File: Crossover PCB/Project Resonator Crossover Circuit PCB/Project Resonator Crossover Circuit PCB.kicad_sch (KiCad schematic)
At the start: 24 parts

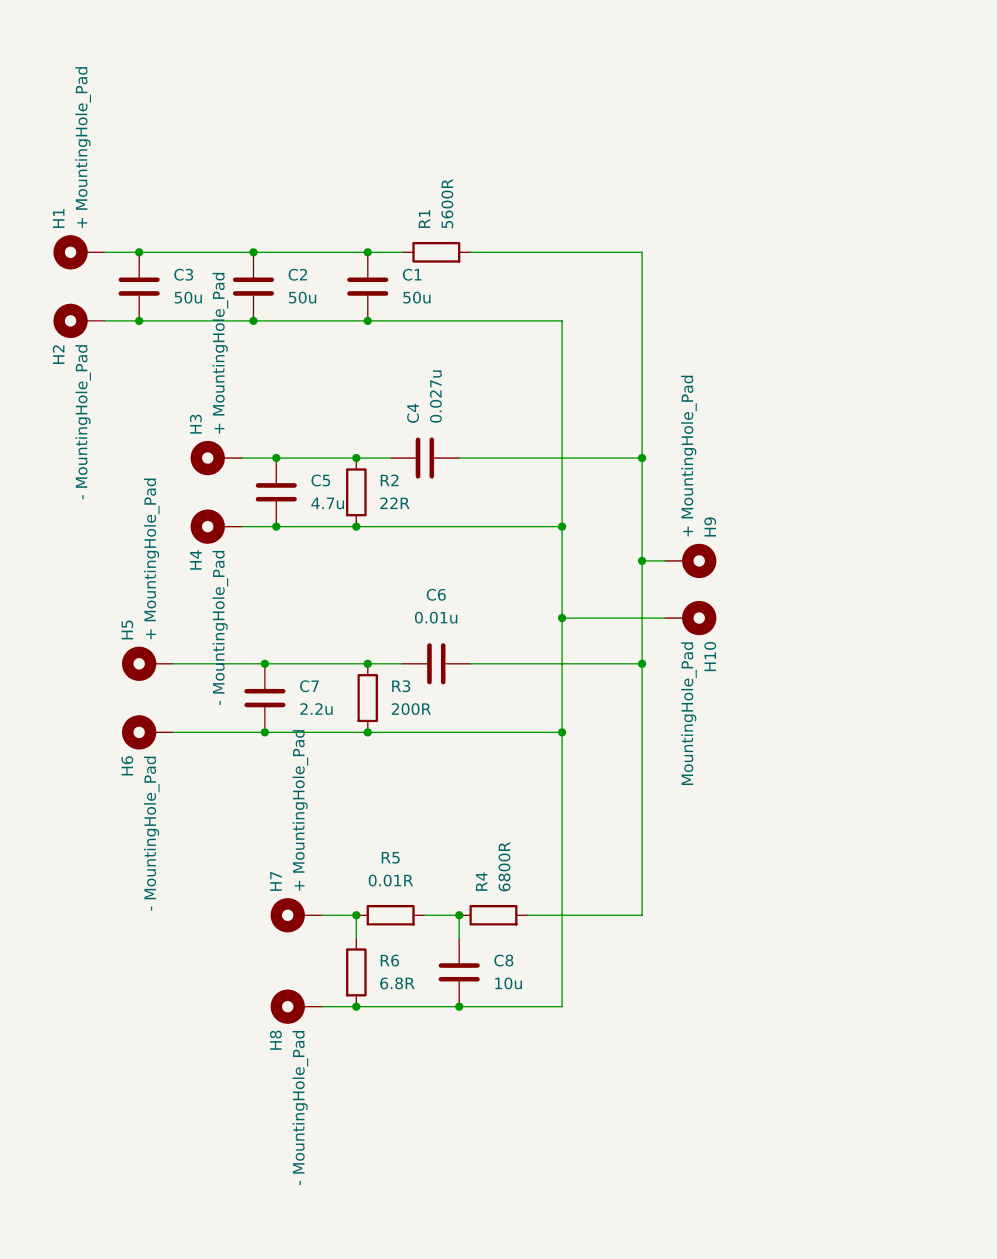
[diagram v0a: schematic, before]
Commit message: MAJOR UPDATE: Improved Crossover to reduce redudent componets from 15 -> 10, Improved subbass isolation, updated PCB to reflect changes, added v3 shell images to assets, uploaded new gerber and drill files
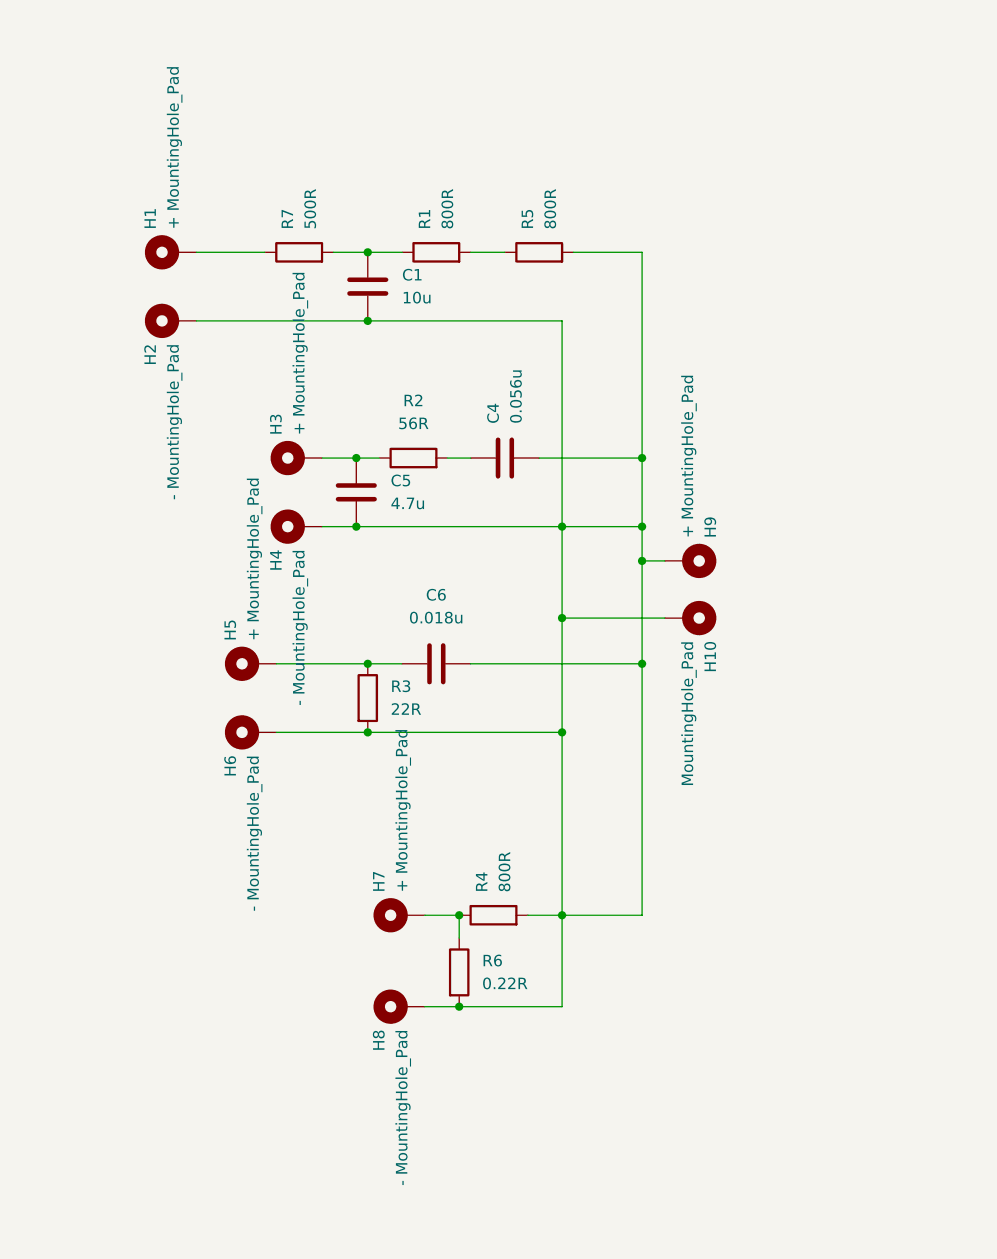
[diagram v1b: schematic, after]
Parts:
- removed C2, C3: 50u, Capacitor_SMD:C_0402_1005Metric_Pad0.74x0.62mm_HandSolder, symbol Device:C
- removed C7: 2.2u, Capacitor_SMD:C_0402_1005Metric_Pad0.74x0.62mm_HandSolder, symbol Device:C
- removed C8: 10u, Capacitor_SMD:C_0402_1005Metric_Pad0.74x0.62mm_HandSolder, symbol Device:C
- added R7: 500R, Resistor_SMD:R_0402_1005Metric_Pad0.72x0.64mm_HandSolder, symbol Device:R
- C1: value 50u -> 10u
- C4: value 0.027u -> 0.056u
- C6: value 0.01u -> 0.018u
- R1: value 5600R -> 800R
- R2: value 22R -> 56R
- R3: value 200R -> 22R
- R4: value 6800R -> 800R
- R5: value 0.01R -> 800R
- R6: value 6.8R -> 0.22R
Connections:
- net at C1.2, C5.2, H10.1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: now also C4.2, C6.2, H9.1, R4.2, R5.2; no longer R2.2
- net at H7.1, R6.1: now also R4.1; no longer R5.1
- net at C5.1, H3.1, R2.1: no longer C4.1
- net at C1.1, R1.1: now also R7.2; no longer H1.1
- new net: C4.1, R2.2
- new net: H1.1, R7.1
- new net: R1.2, R5.1
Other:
- moved on the sheet: C4, C5, H1, H2, H3, H4, H5, H6, H7, H8, R2, R6

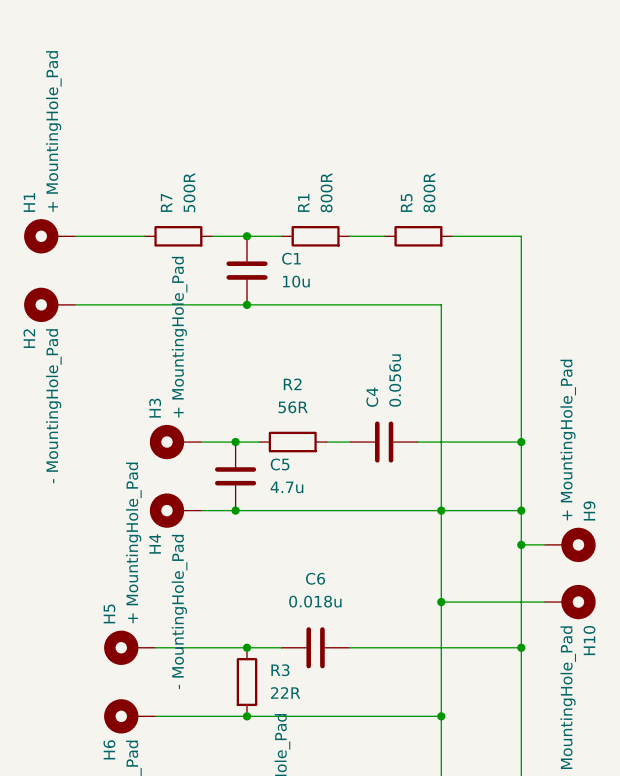
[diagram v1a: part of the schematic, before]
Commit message: updated crossover to have ~5-6db cut at 10k to match shell material high frequency resonace (updated CROSSOVER, SCHEMATIC, PCB, GERBER, and DRILL FILES
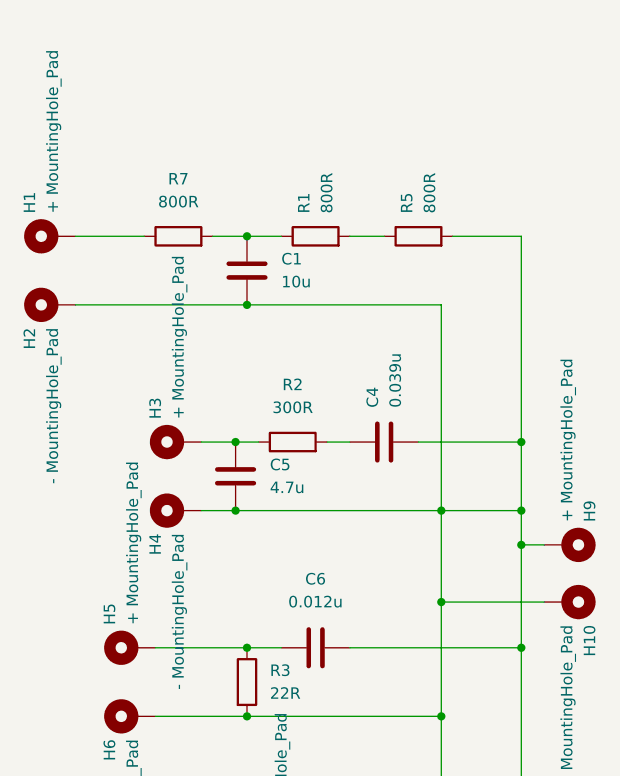
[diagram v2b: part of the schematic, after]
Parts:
- C4: value 0.056u -> 0.039u
- C6: value 0.018u -> 0.012u
- R2: value 56R -> 300R
- R7: value 500R -> 800R
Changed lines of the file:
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@@
 			)
 		)
-		(property "Value" "56R"
+		(property "Value" "300R"
 			(at 149.86 72.39 90)
 			(effects
@@
 		(fields_autoplaced yes)
 		(property "Reference" "R7"
-			(at 135.8899 50.8 0)
-			(effects
-				(font
-					(size 1.27 1.27)
-				)
-				(justify left)
-			)
-		)
-		(property "Value" "500R"
-			(at 138.4299 50.8 0)
-			(effects
-				(font
-					(size 1.27 1.27)
-				)
-				(justify left)
+			(at 137.16 46.99 90)
+			(effects
+				(font
+					(size 1.27 1.27)
+				)
+			)
+		)
+		(property "Value" "800R"
+			(at 137.16 49.53 90)
+			(effects
+				(font
+					(size 1.27 1.27)
+				)
 			)
 		)
@@
 			)
 		)
-		(property "Value" "0.018u"
+		(property "Value" "0.012u"
 			(at 152.4 93.98 90)
 			(effects
@@
 			)
 		)
-		(property "Value" "0.056u"
+		(property "Value" "0.039u"
 			(at 161.2899 72.39 0)
 			(effects

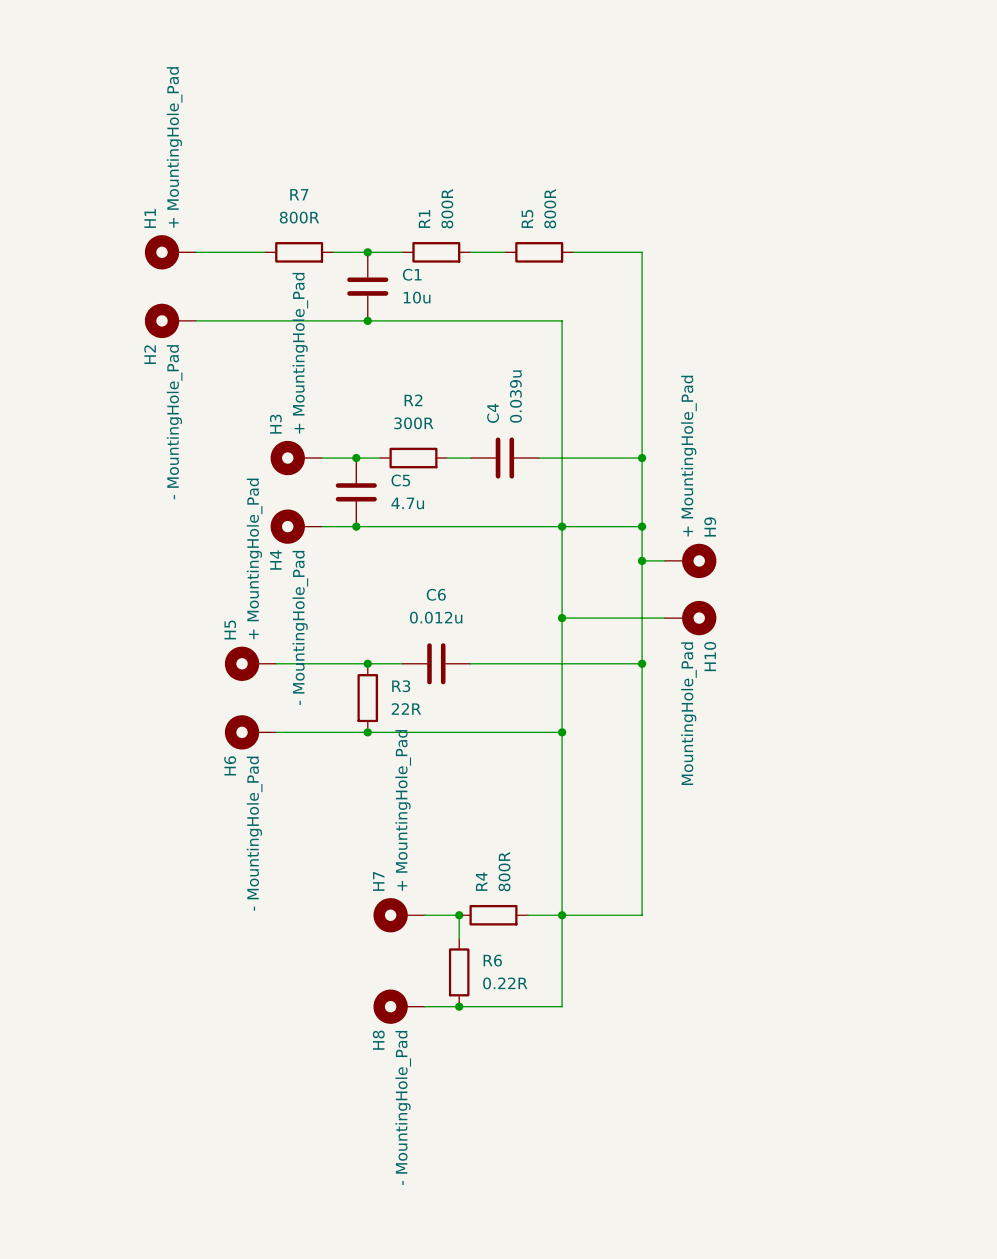
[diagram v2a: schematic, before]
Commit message: updated 800ohm to 750ohm for product resistor in use from JLCPCB, updated ground and added 1 more resistor for CI driver, updated gerber and drill files and updated crossover ciruit to match changes
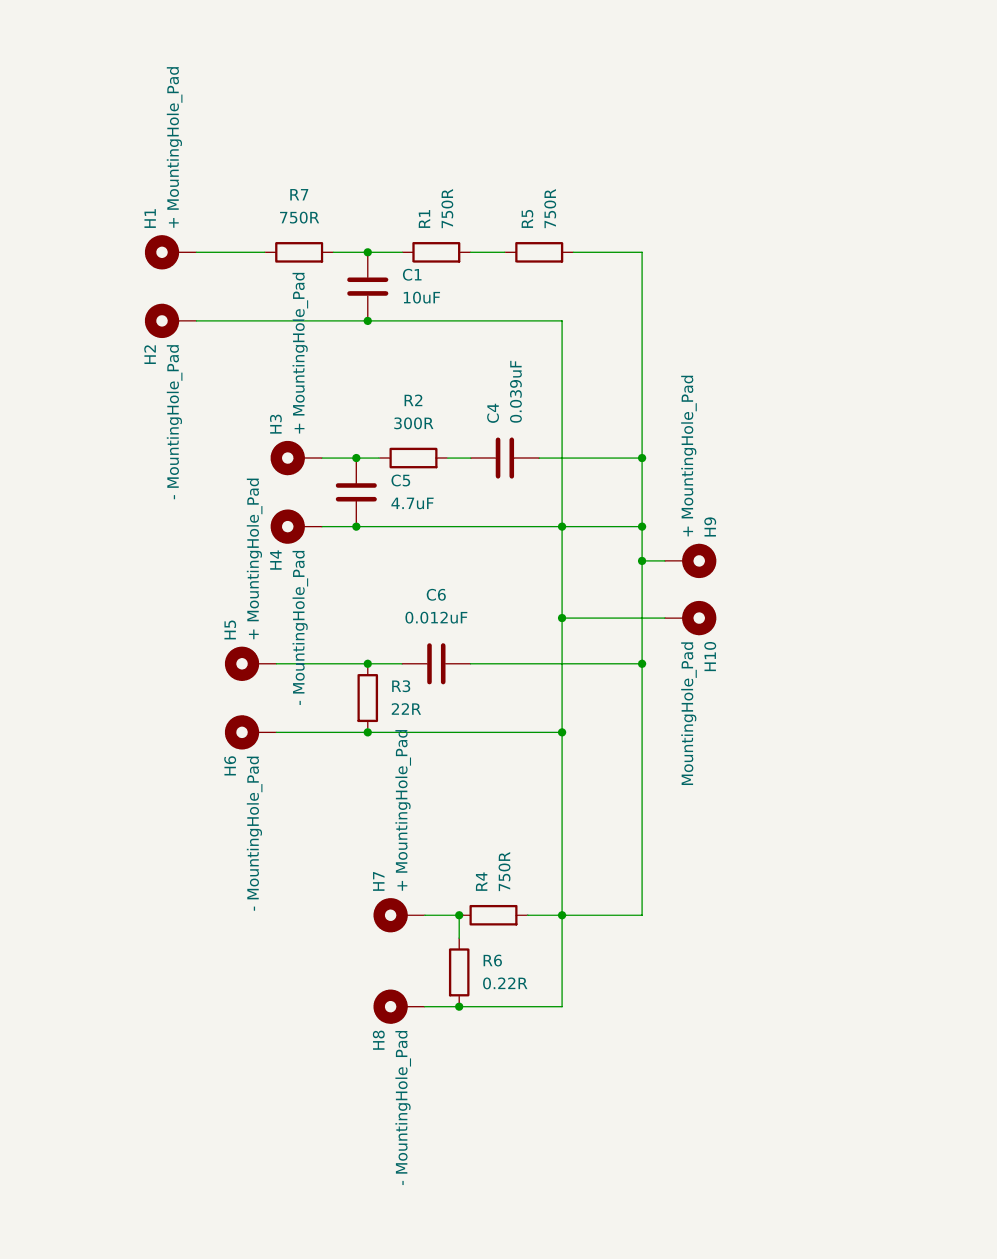
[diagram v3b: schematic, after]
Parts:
- C1: value 10u -> 10uF
- C4: value 0.039u -> 0.039uF
- C5: value 4.7u -> 4.7uF
- C6: value 0.012u -> 0.012uF
- R1, R4, R5, R7: value 800R -> 750R
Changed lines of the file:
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@@
 			)
 		)
-		(property "Value" "4.7u"
+		(property "Value" "4.7uF"
 			(at 147.32 81.2799 0)
 			(effects
@@
 			)
 		)
-		(property "Value" "10u"
+		(property "Value" "10uF"
 			(at 148.59 58.4199 0)
 			(effects
@@
 			)
 		)
-		(property "Value" "800R"
+		(property "Value" "750R"
 			(at 165.0999 50.8 0)
 			(effects
@@
 			)
 		)
-		(property "Value" "800R"
+		(property "Value" "750R"
 			(at 137.16 49.53 90)
 			(effects
@@
 			)
 		)
-		(property "Value" "800R"
+		(property "Value" "750R"
 			(at 153.6699 50.8 0)
 			(effects
@@
 			)
 		)
-		(property "Value" "0.012u"
+		(property "Value" "0.012uF"
 			(at 152.4 93.98 90)
 			(effects
@@
 			)
 		)
-		(property "Value" "0.039u"
+		(property "Value" "0.039uF"
 			(at 161.2899 72.39 0)
 			(effects
@@
 			)
 		)
-		(property "Value" "800R"
+		(property "Value" "750R"
 			(at 160.0199 124.46 0)
 			(effects
